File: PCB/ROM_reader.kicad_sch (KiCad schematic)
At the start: 47 parts, among them J1 USB_B_Mini, J2 TTL_UART, J3 ISP, J4 RAM ADAPTER EXT, U1 CH340G, U2 ATmega128A-A, Y1 12MHz

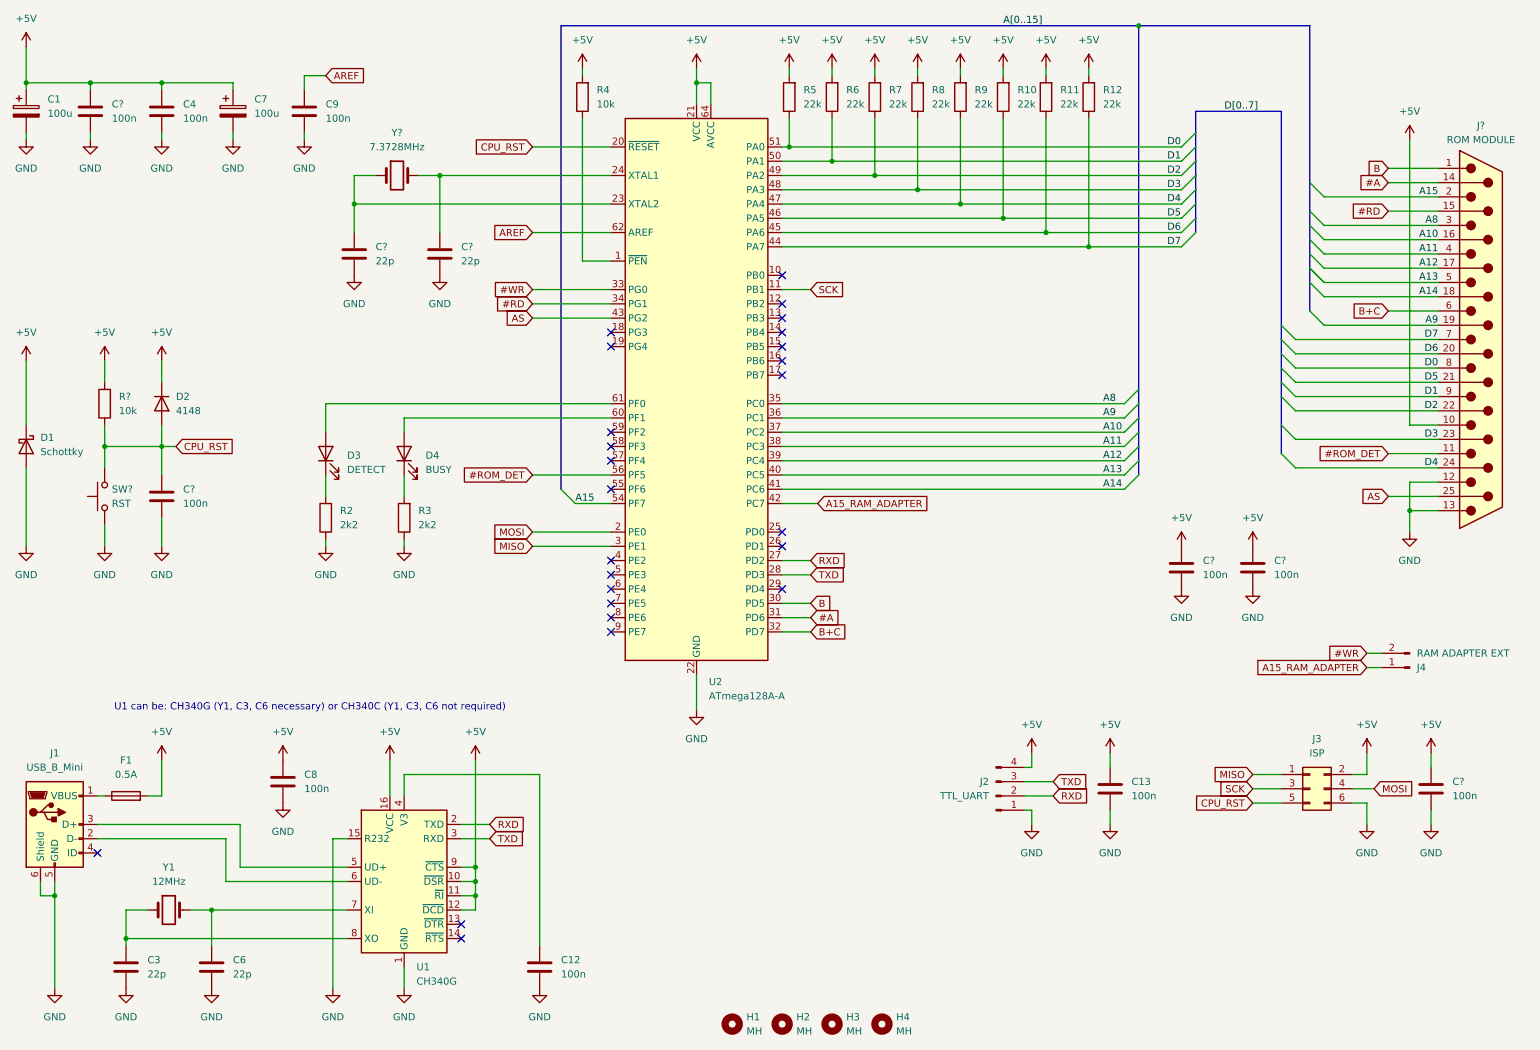
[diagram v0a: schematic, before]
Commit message: miniUSB socket replaced with USB C socket. PCB now at revision D
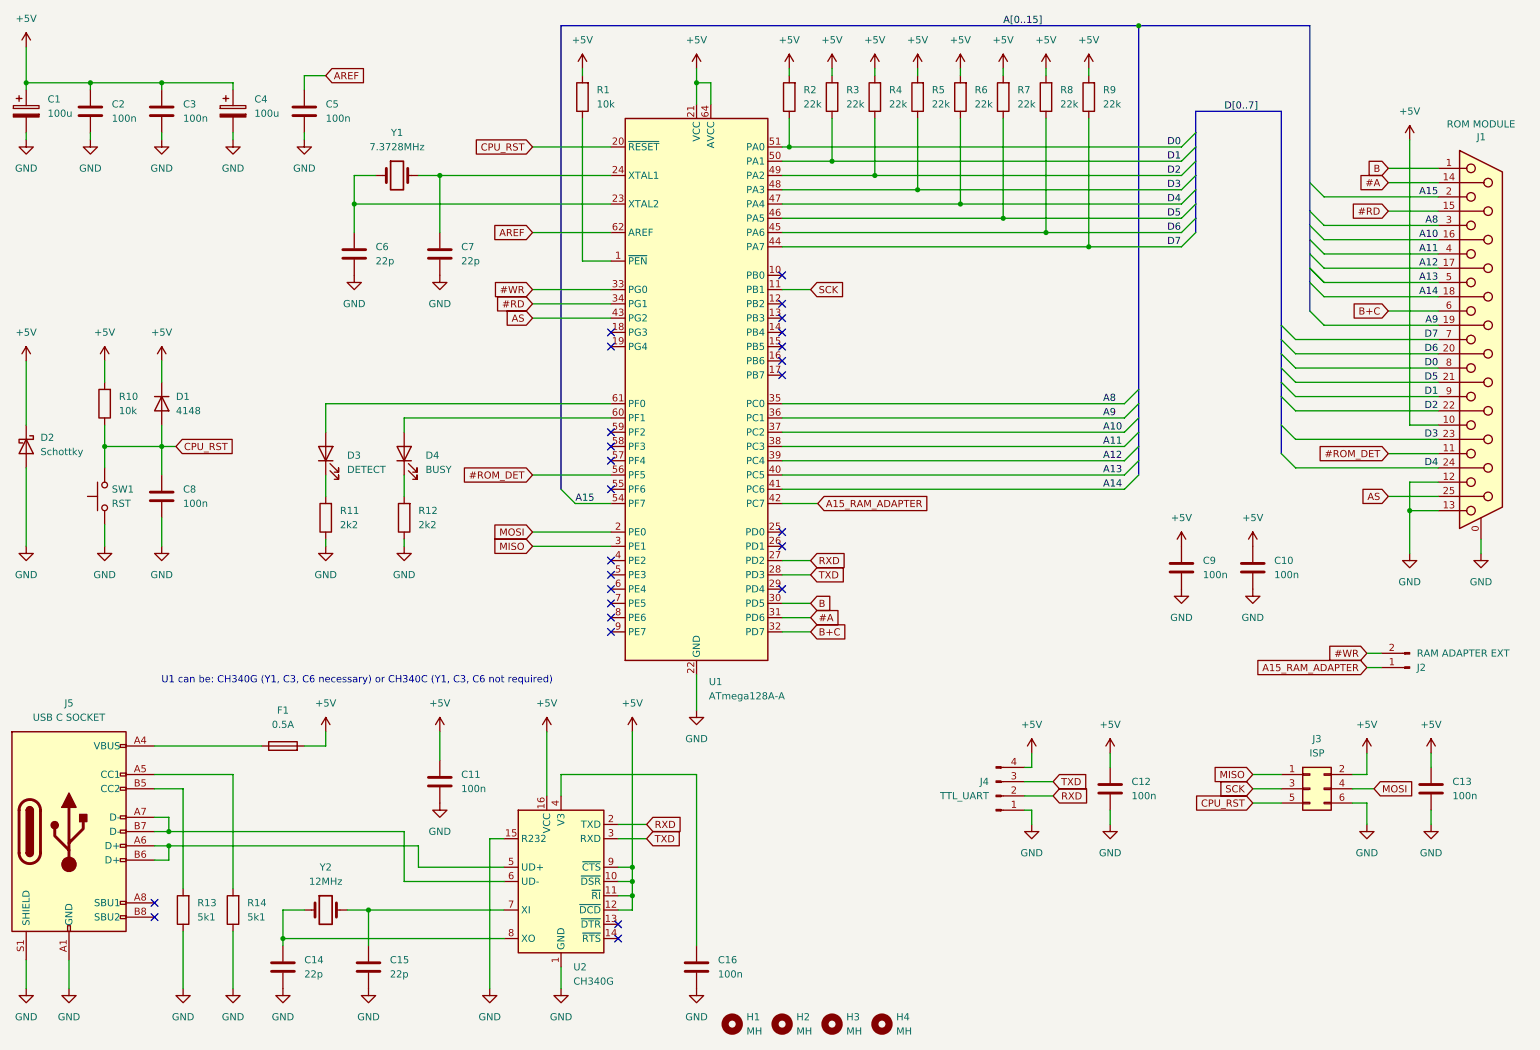
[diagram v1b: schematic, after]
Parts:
- removed J1: USB_B_Mini, Connector_USB:USB_Mini-B_Wuerth_65100516121_Horizontal, symbol Connector:USB_B_Mini
- added J5: USB C SOCKET, Connector_USB:USB_C_Receptacle_GCT_USB4105-xx-A_16P_TopMnt_Horizontal, symbol Connector:USB_C_Receptacle_USB2.0_16P
- added R13, R14: 5k1, Resistor_SMD:R_1206_3216Metric_Pad1.30x1.75mm_HandSolder, symbol Device:R
- J1: renamed from J?; footprint Connector_Dsub:DSUB-25_Female_Horizontal_P2.77x2.84mm_EdgePinOffset4.94mm_Housed_MountingHolesOffset7.48mm -> Connector_Dsub:DSUB-25_Socket_Horizontal_P2.77x2.84mm_EdgePinOffset4.94mm_Housed_MountingHolesOffset4.94mm; symbol Connector:DB25_Plug -> Connector:DB25_Socket_MountingHoles
- gave numbers to parts that had none: 10
- renumbered C8 to C11, C13 to C12, C3 to C14, C6 to C15, C12 to C16, C4 to C3, C7 to C4, C9 to C5, D2 to D1, D1 to D2, J4 to J2, J2 to J4, R4 to R1, R2 to R11, R3 to R12, R5 to R2, R6 to R3, R7 to R4, R8 to R5, R9 to R6, R10 to R7, R11 to R8, R12 to R9, U2 to U1, U1 to U2, Y1 to Y2
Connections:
- net GND: now also J1.0 (PAD), J5.A1 (GND), J5.A12 (GND), J5.B1 (GND), J5.B12 (GND), J5.S1 (SHIELD), R13.1, R14.1
- net at U2.5 (UD+): now also J5.A6 (D+), J5.B6 (D+)
- net at U2.6 (UD-): now also J5.A7 (D-), J5.B7 (D-)
- net at F1.1: now also J5.A4 (VBUS), J5.A9 (VBUS), J5.B4 (VBUS), J5.B9 (VBUS)
- new net: J5.B5 (CC2), R13.2
- new net: J5.A5 (CC1), R14.2
- no-connect marks 25 -> 26
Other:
- moved on the sheet: C11, C14, C15, C16, F1, U2, Y2
